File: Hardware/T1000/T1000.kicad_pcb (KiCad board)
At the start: 4 copper layers, 1 part, among them U4 MAX77857

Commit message: started layout
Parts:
- added AE1: Antenna, Terminator_Lib:ANT_1575AT_JOT-M, F.Cu at (83.6, 80.6)
- added B1: KMR2, Button_Switch_SMD:SW_Push_1P1T_NO_CK_KMR2, F.Cu at (54.8, 70.9)
- added B2: KMR2, Button_Switch_SMD:SW_Push_1P1T_NO_CK_KMR2, F.Cu at (54.8, 75.6)
- added BZ1: Buzzer, Terminator_Lib:PKMCS0909E4000-R1_MUR, F.Cu at (104.7, 102.7)
- added C1: 100nF, Capacitor_SMD:C_0402_1005Metric_Pad0.74x0.62mm_HandSolder, F.Cu at (98.4, 68.2)
- added C10: 100nF, Capacitor_SMD:C_0402_1005Metric_Pad0.74x0.62mm_HandSolder, F.Cu at (101.6, 70.1)
- added C11: 2.2uF, Capacitor_SMD:C_0603_1608Metric_Pad1.08x0.95mm_HandSolder, F.Cu at (80.2, 26.4)
- added C12: 100nF, Capacitor_SMD:C_0402_1005Metric_Pad0.74x0.62mm_HandSolder, F.Cu at (101.6, 72.1)
- added C13: 100nF, Capacitor_SMD:C_0402_1005Metric_Pad0.74x0.62mm_HandSolder, F.Cu at (101.6, 74.1)
- added C14: 100nF, Capacitor_SMD:C_0402_1005Metric_Pad0.74x0.62mm_HandSolder, F.Cu at (101.6, 76.0)
- added C15: 10uF, Capacitor_SMD:C_0603_1608Metric_Pad1.08x0.95mm_HandSolder, F.Cu at (80.2, 28.9)
- added C16: 100nF, Capacitor_SMD:C_0603_1608Metric_Pad1.08x0.95mm_HandSolder, F.Cu at (80.2, 31.4)
- added C17: 1uF, Capacitor_SMD:C_0603_1608Metric_Pad1.08x0.95mm_HandSolder, F.Cu at (80.2, 34.0)
- added C18: 10uF, Capacitor_SMD:C_0603_1608Metric_Pad1.08x0.95mm_HandSolder, F.Cu at (80.2, 36.5)
- added C19: 10uF, Capacitor_SMD:C_0603_1608Metric_Pad1.08x0.95mm_HandSolder, F.Cu at (80.2, 39.0)
- added C2: 22pF, Capacitor_SMD:C_0603_1608Metric_Pad1.08x0.95mm_HandSolder, F.Cu at (80.2, 21.4)
- added C20: 10uF, Capacitor_SMD:C_0603_1608Metric_Pad1.08x0.95mm_HandSolder, F.Cu at (80.2, 41.5)
- added C21: 100nF, Capacitor_SMD:C_0603_1608Metric_Pad1.08x0.95mm_HandSolder, F.Cu at (80.2, 44.0)
- added C22: 220nF, Capacitor_SMD:C_0603_1608Metric_Pad1.08x0.95mm_HandSolder, F.Cu at (80.2, 46.5)
- added C23: 220nF, Capacitor_SMD:C_0603_1608Metric_Pad1.08x0.95mm_HandSolder, F.Cu at (80.2, 49.0)
- added C24: 10pF, Capacitor_SMD:C_0603_1608Metric_Pad1.08x0.95mm_HandSolder, F.Cu at (84.5, 21.4)
- added C25: 2.2uF, Capacitor_SMD:C_0603_1608Metric_Pad1.08x0.95mm_HandSolder, F.Cu at (84.5, 23.9)
- added C26: 470nF, Capacitor_SMD:C_0603_1608Metric_Pad1.08x0.95mm_HandSolder, F.Cu at (84.5, 26.4)
- added C27: 10uF, Capacitor_SMD:C_0603_1608Metric_Pad1.08x0.95mm_HandSolder, F.Cu at (84.5, 28.9)
- added C28: 10uF, Capacitor_SMD:C_0603_1608Metric_Pad1.08x0.95mm_HandSolder, F.Cu at (84.5, 31.4)
- added C29: 15uF, Capacitor_SMD:C_0603_1608Metric_Pad1.08x0.95mm_HandSolder, F.Cu at (84.5, 34.0)
- added C3: 22pF, Capacitor_SMD:C_0603_1608Metric_Pad1.08x0.95mm_HandSolder, F.Cu at (80.2, 23.9)
- added C30: 10uF, Capacitor_SMD:C_0603_1608Metric_Pad1.08x0.95mm_HandSolder, F.Cu at (84.5, 36.5)
- added C31: 2.2uF, Capacitor_SMD:C_0603_1608Metric_Pad1.08x0.95mm_HandSolder, F.Cu at (84.5, 39.0)
- added C32: 220nF, Capacitor_SMD:C_0603_1608Metric_Pad1.08x0.95mm_HandSolder, F.Cu at (165.8, 82.9)
- added C33: 220nF, Capacitor_SMD:C_0603_1608Metric_Pad1.08x0.95mm_HandSolder, F.Cu at (156.1, 82.9)
- added C34: 4.7uF, Capacitor_SMD:C_0603_1608Metric_Pad1.08x0.95mm_HandSolder, F.Cu at (161.7, 94.1)
- added C35: 100nF, Capacitor_SMD:C_0603_1608Metric_Pad1.08x0.95mm_HandSolder, F.Cu at (84.5, 49.0)
- added C36: 47pF, Capacitor_SMD:C_0603_1608Metric_Pad1.08x0.95mm_HandSolder, F.Cu at (88.9, 21.4)
- added C37: 8.2pF, Capacitor_SMD:C_0603_1608Metric_Pad1.08x0.95mm_HandSolder, F.Cu at (88.9, 23.9)
- added C38: 22nF, Capacitor_SMD:C_0603_1608Metric_Pad1.08x0.95mm_HandSolder, F.Cu at (88.9, 26.4)
- added C39: 22uF, Capacitor_SMD:C_0603_1608Metric_Pad1.08x0.95mm_HandSolder, F.Cu at (155.2, 86.3)
- added C4: 100nF, Capacitor_SMD:C_0402_1005Metric_Pad0.74x0.62mm_HandSolder, F.Cu at (98.4, 70.1)
- added C40: 22uF, Capacitor_SMD:C_0603_1608Metric_Pad1.08x0.95mm_HandSolder, F.Cu at (155.2, 87.9)
- added C41: 680p, Capacitor_SMD:C_0603_1608Metric_Pad1.08x0.95mm_HandSolder, F.Cu at (160.1, 95.0)
- added C42: 10uF, Capacitor_SMD:C_0603_1608Metric_Pad1.08x0.95mm_HandSolder, F.Cu at (165.1, 86.8)
- added C5: 1uF, Capacitor_SMD:C_0402_1005Metric_Pad0.74x0.62mm_HandSolder, F.Cu at (98.4, 72.1)
- added C6: 1uF, Capacitor_SMD:C_0402_1005Metric_Pad0.74x0.62mm_HandSolder, F.Cu at (98.4, 74.1)
- added C7: 100nF, Capacitor_SMD:C_0402_1005Metric_Pad0.74x0.62mm_HandSolder, F.Cu at (98.4, 76.0)
- added C8: 100nF, Capacitor_SMD:C_0402_1005Metric_Pad0.74x0.62mm_HandSolder, F.Cu at (98.4, 78.0)
- added C9: 100nF, Capacitor_SMD:C_0402_1005Metric_Pad0.74x0.62mm_HandSolder, F.Cu at (101.6, 68.2)
- added D1: LED, Diode_SMD:D_0603_1608Metric_Pad1.05x0.95mm_HandSolder, F.Cu at (99.0, 80.3)
- added D2: USBLC6-2SC6, PCM_Package_TO_SOT_SMD_AKL:SOT-23-6, F.Cu at (106.9, 36.0)
- added J1: USB_C_Receptacle_USB2.0, Connector_USB:USB_C_Receptacle_GCT_USB4085, F.Cu at (67.1, 58.5)
- added J2: SOICbite, Terminator_Lib:SOIC_clipProgSmall, F.Cu at (62.4, 81.0)
- added J3: XT30, Connector_AMASS:AMASS_XT30PW-M_1x02_P2.50mm_Horizontal, F.Cu at (103.9, 64.4)
- added J4: Nichrome, Connector_PinHeader_2.54mm:PinHeader_1x02_P2.54mm_Vertical, F.Cu at (105.5, 69.5)
- added JP1: SolderJumper_2_Open, Jumper:SolderJumper-2_P1.3mm_Open_TrianglePad1.0x1.5mm, F.Cu at (163.6, 97.6)
- added JP2: SolderJumper_2_Open, Jumper:SolderJumper-2_P1.3mm_Open_TrianglePad1.0x1.5mm, F.Cu at (163.6, 100.5)
- added L1: 1.5uH, Inductor_SMD:L_Vishay_IHLP-2020, F.Cu at (103.9, 30.2)
- added L2: 3.3uH, Terminator_Lib:L_Bourns_SRP1265A, F.Cu at (160.9, 75.5)
- added L3: 3.3uH, Terminator_Lib:L_Bourns_SRP1265A, F.Cu at (85.9, 71.3)
- added Q1: IRLML0060TRPBF, Package_TO_SOT_SMD:SOT-23-3, F.Cu at (102.3, 47.9)
- added R1: DNP, Resistor_SMD:R_0603_1608Metric_Pad0.98x0.95mm_HandSolder, F.Cu at (88.9, 36.5)
- added R10: 154k, Resistor_SMD:R_0603_1608Metric_Pad0.98x0.95mm_HandSolder, F.Cu at (93.2, 28.9)
- added R11: 10k, Resistor_SMD:R_0603_1608Metric_Pad0.98x0.95mm_HandSolder, F.Cu at (93.2, 31.4)
- added R12: 10k, Resistor_SMD:R_0603_1608Metric_Pad0.98x0.95mm_HandSolder, F.Cu at (93.2, 34.0)
- added R13: 10k, Resistor_SMD:R_0603_1608Metric_Pad0.98x0.95mm_HandSolder, F.Cu at (93.2, 36.5)
- added R14: 5.1k, Resistor_SMD:R_0603_1608Metric_Pad0.98x0.95mm_HandSolder, F.Cu at (93.2, 39.0)
- added R15: 5.1k, Resistor_SMD:R_0603_1608Metric_Pad0.98x0.95mm_HandSolder, F.Cu at (93.2, 41.5)
- added R16: 510k, Resistor_SMD:R_0603_1608Metric_Pad0.98x0.95mm_HandSolder, F.Cu at (93.2, 44.0)
- added R17: 16.9k, Resistor_SMD:R_0603_1608Metric_Pad0.98x0.95mm_HandSolder, F.Cu at (93.2, 46.5)
- added R18: 178k, Resistor_SMD:R_0603_1608Metric_Pad0.98x0.95mm_HandSolder, F.Cu at (93.2, 49.0)
- added R19: 20k, Resistor_SMD:R_0603_1608Metric_Pad0.98x0.95mm_HandSolder, F.Cu at (97.6, 21.4)
- added R2: 10k, Resistor_SMD:R_0603_1608Metric_Pad0.98x0.95mm_HandSolder, F.Cu at (88.9, 39.0)
- added R20: 100m, Resistor_SMD:R_0603_1608Metric_Pad0.98x0.95mm_HandSolder, F.Cu at (97.6, 23.9)
- added R21: 33, Resistor_SMD:R_0603_1608Metric_Pad0.98x0.95mm_HandSolder, F.Cu at (97.6, 26.4)
- added R22: 33, Resistor_SMD:R_0603_1608Metric_Pad0.98x0.95mm_HandSolder, F.Cu at (97.6, 28.9)
- added R23: 81.1k, Resistor_SMD:R_0603_1608Metric_Pad0.98x0.95mm_HandSolder, F.Cu at (156.1, 92.0)
- added R24: 75k, Resistor_SMD:R_0603_1608Metric_Pad0.98x0.95mm_HandSolder, F.Cu at (163.3, 94.1)
- added R25: 5m, Resistor_SMD:R_0603_1608Metric_Pad0.98x0.95mm_HandSolder, F.Cu at (155.5, 90.4)
- added R26: 154k, Resistor_SMD:R_0603_1608Metric_Pad0.98x0.95mm_HandSolder, F.Cu at (155.9, 95.8)
- added R27: 154k, Resistor_SMD:R_0603_1608Metric_Pad0.98x0.95mm_HandSolder, F.Cu at (155.9, 94.2)
- added R28: 56.2k, Resistor_SMD:R_0603_1608Metric_Pad0.98x0.95mm_HandSolder, F.Cu at (158.5, 95.0)
- added R29: 100, Resistor_SMD:R_0603_1608Metric_Pad0.98x0.95mm_HandSolder, F.Cu at (101.3, 109.4)
- added R3: 1M, Resistor_SMD:R_0603_1608Metric_Pad0.98x0.95mm_HandSolder, F.Cu at (88.9, 41.5)
- added R4: 715k, Resistor_SMD:R_0603_1608Metric_Pad0.98x0.95mm_HandSolder, F.Cu at (88.9, 44.0)
- added R5: 27, Resistor_SMD:R_0603_1608Metric_Pad0.98x0.95mm_HandSolder, F.Cu at (88.9, 46.5)
- added R6: 27, Resistor_SMD:R_0603_1608Metric_Pad0.98x0.95mm_HandSolder, F.Cu at (88.9, 49.0)
- added R7: 590, Resistor_SMD:R_0603_1608Metric_Pad0.98x0.95mm_HandSolder, F.Cu at (93.2, 21.4)
- added R8: 1k, Resistor_SMD:R_0603_1608Metric_Pad0.98x0.95mm_HandSolder, F.Cu at (93.2, 23.9)
- added R9: 1.05M, Resistor_SMD:R_0603_1608Metric_Pad0.98x0.95mm_HandSolder, F.Cu at (93.2, 26.4)
- added TP1: TestPoint, TestPoint:TestPoint_Pad_D1.0mm, F.Cu at (95.3, 68.7)
- added TP2: TestPoint, TestPoint:TestPoint_Keystone_5000-5004_Miniature, F.Cu at (91.0, 80.5)
- added TP3: TestPoint, TestPoint:TestPoint_Pad_D1.0mm, F.Cu at (95.3, 71.8)
- added TP4: TestPoint, TestPoint:TestPoint_Pad_D1.0mm, F.Cu at (95.3, 74.8)
- added TP5: TestPoint, TestPoint:TestPoint_Pad_D1.0mm, F.Cu at (95.3, 77.8)
- added TP6: TestPoint, TestPoint:TestPoint_Pad_D1.0mm, F.Cu at (95.3, 80.9)
- added U1: LT3120JV-PBF, Terminator_Lib:LQFN28_Rev0_ADI-M, F.Cu at (160.9, 88.8)
- added U2: RP2040, Terminator_Lib:RP2040-QFN-56, F.Cu at (30.8, 93.0)
- added U3: W25Q128JVS, Package_SO:SOIC-8_5.23x5.23mm_P1.27mm, F.Cu at (104.9, 23.5)
- added U5: MAX-M10S, RF_GPS:ublox_MAX, F.Cu at (57.9, 62.8)
- added U6: MS5607-02BA, Package_LGA:LGA-8_3x5mm_P1.25mm, F.Cu at (102.1, 36.9)
- added U7: LT6703CDC-3, PCM_Package_DFN_QFN_AKL:DFN-3-1EP-2x2mm_P0.5mm_EP1x1.35mm, F.Cu at (53.7, 79.8)
- added U8: MAX77857, Terminator_Lib:MAX77857-35WLP, F.Cu at (133.5, 57.8)
- added U9: XBee_SMT, RF_Module:Digi_XBee_SMT, F.Cu at (38.4, 35.7)
- added Y1: 445I23D12M00000, Crystal:Crystal_SMD_5032-2Pin_5.0x3.2mm, F.Cu at (71.0, 79.0)
- U4: value MAX77857 -> LTC4419; footprint Package_BGA:MAX77857-35WLP -> Package_SO:MSOP-12-1EP_3x4mm_P0.65mm_EP1.65x2.85mm_ThermalVias
- moved U4 62.0 mm to (103.4, 42.9)
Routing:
- net Net-(U1-ISN): track 0.00 -> 12.3 mm, vias 0 -> 2
- net GND: track 0.00 -> 9.27 mm
- net Net-(J4-Pin_1): track 0.00 -> 9.15 mm
- net Net-(U1-BST1): track 0.00 -> 6.04 mm
- net Net-(U1-BST2): track 0.00 -> 6.03 mm
- net Net-(U1-FB): track 0.00 -> 5.89 mm
- net +BATT: track 0.00 -> 4.85 mm
- net Net-(U1-VC): track 0.00 -> 3.35 mm
- net Net-(U1-PROG): track 0.00 -> 2.47 mm
- net Net-(U1-MPCC): track 0.00 -> 2.34 mm
- net Net-(U1-RT): track 0.00 -> 2.24 mm
- net Net-(C41-Pad1): track 0.00 -> 1.62 mm
- net (no net): track 0.63 -> 0.00 mm
- added copper zone on F.Cu, net Net-(C32-Pad2)
- added copper zone on F.Cu, net Net-(C33-Pad2)
- added copper zone on F.Cu, net Net-(J4-Pin_1)

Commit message: more layout
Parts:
- C1, C10, C12, C13, C14, C4, C5, C6, C7, C8, C9: moved to B.Cu
- C29: footprint Capacitor_SMD:C_0603_1608Metric_Pad1.08x0.95mm_HandSolder -> Capacitor_SMD:C_0805_2012Metric_Pad1.18x1.45mm_HandSolder
- L3: footprint Terminator_Lib:L_Bourns_SRP1265A -> Inductor_SMD:L_1008_2520Metric_Pad1.43x2.20mm_HandSolder
- R20: footprint Resistor_SMD:R_0603_1608Metric_Pad0.98x0.95mm_HandSolder -> Resistor_SMD:R_0805_2012Metric_Pad1.20x1.40mm_HandSolder
- moved U3 118.9 mm to (46.7, 127.2), turned to 90 degrees
- moved C15 91.5 mm to (50.0, 115.3), turned to 90 degrees
- moved C9 73.3 mm to (55.1, 124.8), turned to 90 degrees
- moved C13 69.0 mm to (50.6, 120.6)
- moved C12 69.0 mm to (50.6, 118.6)
- moved C5 68.8 mm to (50.6, 121.6)
- moved C4 68.8 mm to (50.6, 119.6)
- moved L3 68.4 mm to (145.4, 37.7)
- moved C10 68.0 mm to (53.3, 118.0), turned to -90 degrees
- moved C8 66.2 mm to (51.5, 124.8), turned to 90 degrees
- moved C1 66.1 mm to (57.5, 120.1), turned to 180 degrees
- moved C6 63.7 mm to (52.3, 118.0), turned to -90 degrees
- moved C14 62.6 mm to (55.1, 118.0), turned to -90 degrees
- moved C23 61.7 mm to (141.3, 40.6), turned to 180 degrees
- moved C29 61.4 mm to (145.6, 40.2), turned to 180 degrees
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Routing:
- net /QSPI_SS: track 0.00 -> 16.5 mm
- net /QSPI_SD1: track 0.00 -> 14.0 mm
- net Net-(C23-Pad1): track 0.00 -> 13.8 mm, vias 0 -> 13
- net Net-(C22-Pad2): track 0.00 -> 13.8 mm, vias 0 -> 13
- net /QSPI_SD2: track 0.00 -> 9.34 mm
- net Net-(U8-FB): track 0.00 -> 6.11 mm
- net Net-(U8-SEL): track 0.00 -> 6.10 mm
- net +3V3: track 0.00 -> 5.75 mm, vias 0 -> 2
- net /QSPI_SD3: track 0.00 -> 5.45 mm
- net +1V1: track 0.00 -> 4.54 mm, vias 0 -> 2
- net /QSPI_SCLK: track 0.00 -> 3.94 mm
- net GND: track 9.27 -> 12.1 mm
- net /QSPI_SD0: track 0.00 -> 2.37 mm
- net Net-(C24-Pad1): track 0.00 -> 1.62 mm
- net /LVC: track 0.00 -> 0.40 mm, vias 0 -> 1
- added copper zone on F.Cu, net +3V3
- added copper zone on F.Cu, net +VDC
- added copper zone on F.Cu, net GND
- added copper zone on F.Cu, net Net-(C22-Pad2)
- added copper zone on In1.Cu, net Net-(C22-Pad2)
- added copper zone on F.Cu, net Net-(C23-Pad1)
- added copper zone on In1.Cu, net Net-(C23-Pad1)
- added copper zone on F.Cu, net Net-(C24-Pad1)
- added copper zone on F.Cu, net Net-(JP1-B)
- added copper zone on F.Cu, net Net-(U1-ISN)
- added copper zone on F.Cu, net Net-(U8-BST1)
- added copper zone on F.Cu, net Net-(U8-BST2)
- added copper zone on F.Cu, net Net-(U8-SCL)

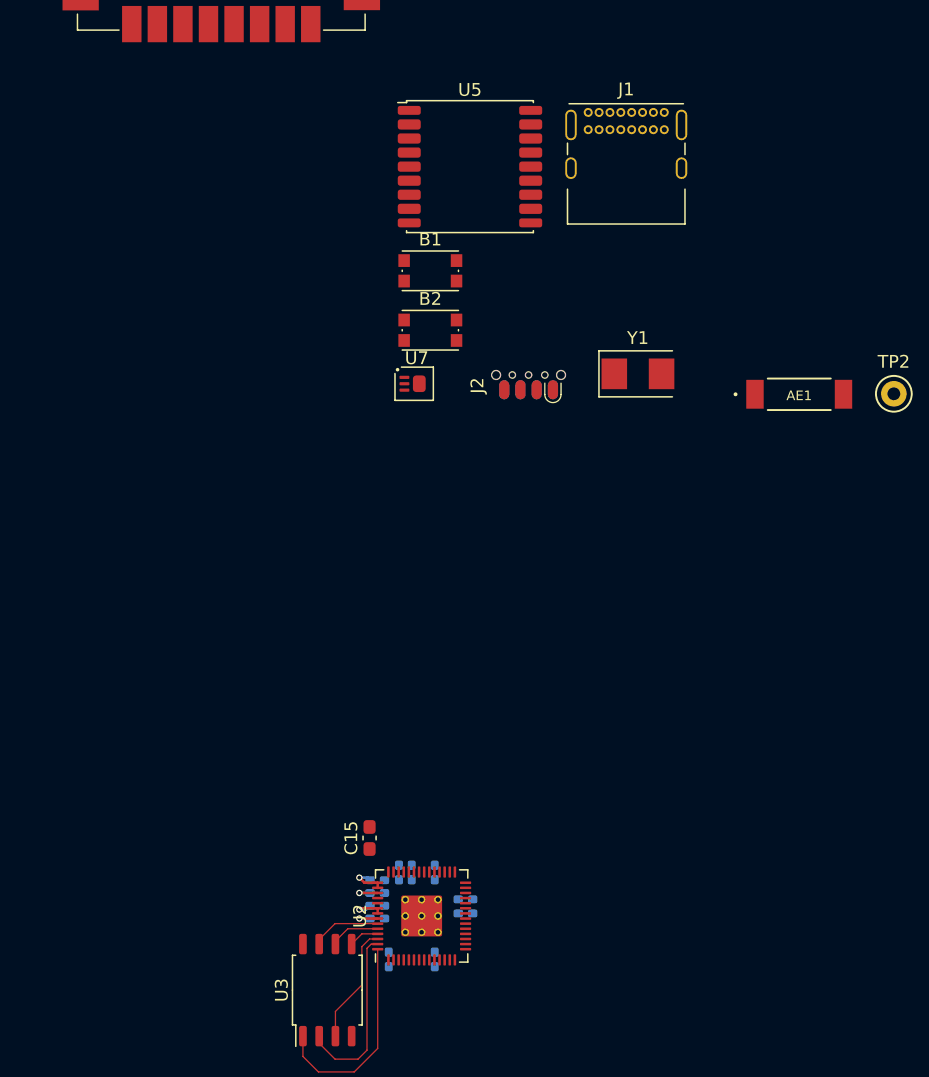
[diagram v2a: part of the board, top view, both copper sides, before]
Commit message: little bit of routing, changed to MIA-M10 GPS to make my life harder
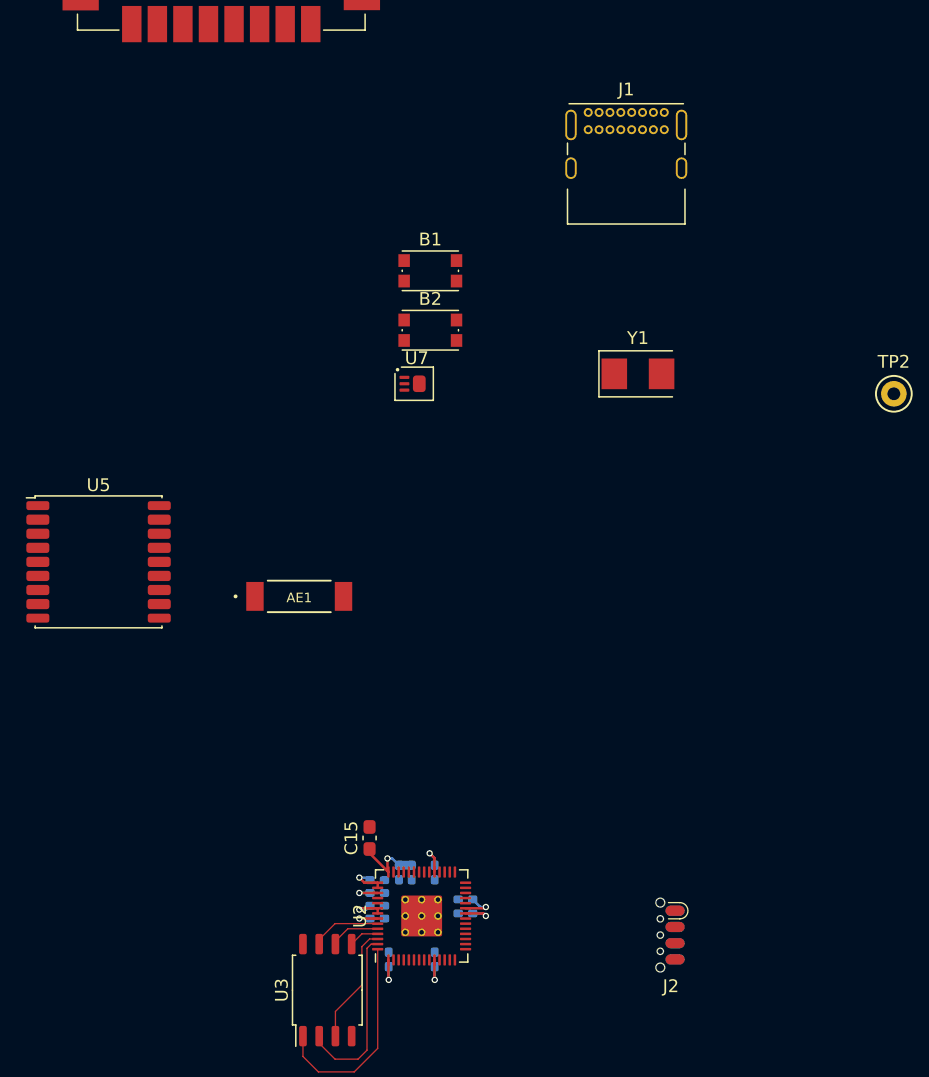
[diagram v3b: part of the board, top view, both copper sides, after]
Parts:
- moved J2 43.7 mm to (74.7, 122.9), turned to 90 degrees
- moved U5 42.4 mm to (28.8, 93.7)
- moved AE1 42.2 mm to (44.5, 96.4)
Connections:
- U2 pad 24: Net-(J2-Pin_2) -> Net-(J2-Pin_3)
- U2 pad 25: Net-(J2-Pin_3) -> Net-(J2-Pin_2)
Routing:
- net +3V3: track 5.75 -> 22.1 mm, vias 2 -> 7
- net +1V1: track 4.54 -> 7.45 mm, vias 2 -> 3
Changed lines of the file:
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@@
   )
   (footprint "Terminator_Lib:SOIC_clipProgSmall" (layer "F.Cu")
-    (at 62.44 80.985)
+    (at 74.65 122.895 90)
     (property "Sheetfile" "T1000.kicad_sch")
     (property "Sheetname" "")
@@
     (property "ki_keywords" "connector")
     (attr through_hole)
-    (fp_text reference "J2" (at -4 -1.0795 -90) (layer "F.SilkS")
+    (fp_text reference "J2" (at -4 -1.0795) (layer "F.SilkS")
         (effects (font (size 1 1) (thickness 0.25)))
     )
-    (fp_text value "SOICbite" (at 0.127 1.397 -180) (layer "F.Fab")
+    (fp_text value "SOICbite" (at 0.127 1.397 90) (layer "F.Fab")
         (effects (font (size 1 1) (thickness 0.15)))
     )
@@
     (fp_line (start 3.175 0.381) (end 3.175 -2.54)
       (stroke (width 0.1) (type solid)) (layer "F.Fab"))
-    (pad "" np_thru_hole circle (at -2.54 -1.905) (size 0.7 0.7) (drill 0.7) (layers "*.Cu" "*.Mask"))
-    (pad "" np_thru_hole circle (at -1.27 -1.905) (size 0.5 0.5) (drill 0.5) (layers "F&B.Cu" "*.Mask"))
-    (pad "" np_thru_hole circle (at 0 -1.905) (size 0.5 0.5) (drill 0.5) (layers "F&B.Cu" "*.Mask"))
-    (pad "" np_thru_hole circle (at 1.27 -1.905) (size 0.5 0.5) (drill 0.5) (layers "F&B.Cu" "*.Mask"))
-    (pad "" np_thru_hole circle (at 2.54 -1.905) (size 0.7 0.7) (drill 0.7) (layers "*.Cu" "*.Mask"))
-    (pad "1" smd oval (at 1.905 -0.75) (size 0.8 1.5) (layers "F.Cu" "F.Mask")
+    (pad "" np_thru_hole circle (at -2.54 -1.905 90) (size 0.7 0.7) (drill 0.7) (layers "*.Cu" "*.Mask"))
+    (pad "" np_thru_hole circle (at -1.27 -1.905 90) (size 0.5 0.5) (drill 0.5) (layers "F&B.Cu" "*.Mask"))
+    (pad "" np_thru_hole circle (at 0 -1.905 90) (size 0.5 0.5) (drill 0.5) (layers "F&B.Cu" "*.Mask"))
+    (pad "" np_thru_hole circle (at 1.27 -1.905 90) (size 0.5 0.5) (drill 0.5) (layers "F&B.Cu" "*.Mask"))
+    (pad "" np_thru_hole circle (at 2.54 -1.905 90) (size 0.7 0.7) (drill 0.7) (layers "*.Cu" "*.Mask"))
+    (pad "1" smd oval (at 1.905 -0.75 90) (size 0.8 1.5) (layers "F.Cu" "F.Mask")
       (net 8 "+3V3") (pinfunction "Pin_1") (pintype "passive"))
-    (pad "2" smd oval (at 0.635 -0.75) (size 0.8 1.5) (layers "F.Cu" "F.Mask")
+    (pad "2" smd oval (at 0.635 -0.75 90) (size 0.8 1.5) (layers "F.Cu" "F.Mask")
       (net 37 "Net-(J2-Pin_2)") (pinfunction "Pin_2") (pintype "passive"))
-    (pad "3" smd oval (at -0.635 -0.75) (size 0.8 1.5) (layers "F.Cu" "F.Mask")
+    (pad "3" smd oval (at -0.635 -0.75 90) (size 0.8 1.5) (layers "F.Cu" "F.Mask")
       (net 38 "Net-(J2-Pin_3)") (pinfunction "Pin_3") (pintype "passive"))
-    (pad "4" smd oval (at -1.905 -0.75) (size 0.8 1.5) (layers "F.Cu" "F.Mask")
+    (pad "4" smd oval (at -1.905 -0.75 90) (size 0.8 1.5) (layers "F.Cu" "F.Mask")
       (net 2 "GND") (pinfunction "Pin_4") (pintype "passive"))
-    (pad "5" smd oval (at -1.905 -0.75) (size 0.8 1.5) (layers "B.Cu" "B.Mask")
+    (pad "5" smd oval (at -1.905 -0.75 90) (size 0.8 1.5) (layers "B.Cu" "B.Mask")
       (net 39 "unconnected-(J2-Pin_5-Pad5)") (pinfunction "Pin_5") (pintype "passive+no_connect"))
-    (pad "6" smd oval (at -0.635 -0.75) (size 0.8 1.5) (layers "B.Cu" "B.Mask")
+    (pad "6" smd oval (at -0.635 -0.75 90) (size 0.8 1.5) (layers "B.Cu" "B.Mask")
       (net 40 "unconnected-(J2-Pin_6-Pad6)") (pinfunction "Pin_6") (pintype "passive+no_connect"))
-    (pad "7" smd oval (at 0.635 -0.75) (size 0.8 1.5) (layers "B.Cu" "B.Mask")
+    (pad "7" smd oval (at 0.635 -0.75 90) (size 0.8 1.5) (layers "B.Cu" "B.Mask")
       (net 41 "unconnected-(J2-Pin_7-Pad7)") (pinfunction "Pin_7") (pintype "passive+no_connect"))
-    (pad "8" smd oval (at 1.905 -0.75) (size 0.8 1.5) (layers "B.Cu" "B.Mask")
+    (pad "8" smd oval (at 1.905 -0.75 90) (size 0.8 1.5) (layers "B.Cu" "B.Mask")
       (net 42 "unconnected-(J2-Pin_8-Pad8)") (pinfunction "Pin_8") (pintype "passive+no_connect"))
   )
@@
       (net 5 "+1V1") (pinfunction "DVDD") (pintype "power_in"))
     (pad "24" smd roundrect (at 1 3.4375 90) (size 0.2 0.875) (layers "F.Cu" "F.Paste" "F.Mask") (roundrect_rratio 0.25)
-      (net 37 "Net-(J2-Pin_2)") (pinfunction "SWCLK") (pintype "output"))
+      (net 38 "Net-(J2-Pin_3)") (pinfunction "SWCLK") (pintype "output"))
     (pad "25" smd roundrect (at 1.4 3.4375 90) (size 0.2 0.875) (layers "F.Cu" "F.Paste" "F.Mask") (roundrect_rratio 0.25)
-      (net 38 "Net-(J2-Pin_3)") (pinfunction "SWD") (pintype "bidirectional"))
+      (net 37 "Net-(J2-Pin_2)") (pinfunction "SWD") (pintype "bidirectional"))
     (pad "26" smd roundrect (at 1.8 3.4375 90) (size 0.2 0.875) (layers "F.Cu" "F.Paste" "F.Mask") (roundrect_rratio 0.25)
       (net 3 "Net-(U2-RUN)") (pinfunction "RUN") (pintype "input"))
@@
   )
   (footprint "RF_GPS:ublox_MAX" (layer "F.Cu")
-    (at 57.855 62.78)
+    (at 28.8 93.7)
     (descr "ublox MAX 6/7/8, (https://www.u-blox.com/sites/default/files/MAX-8-M8-FW3_HardwareIntegrationManual_%28UBX-15030059%29.pdf)")
     (tags "GPS ublox MAX 6/7/8")
@@
   )
   (footprint "Terminator_Lib:ANT_1575AT_JOT-M" (layer "F.Cu")
-    (at 83.613499 80.5891)
+    (at 44.5 96.4)
     (tags "1575AT43A0040E ")
     (property "Sheetfile" "T1000.kicad_sch")
@@
       (polygon
         (pts
-          (xy 80.882999 79.535)
-          (xy 86.343999 79.535)
-          (xy 86.343999 81.6432)
-          (xy 80.882999 81.6432)
+          (xy 41.7695 95.3459)
+          (xy 47.2305 95.3459)
+          (xy 47.2305 97.4541)
+          (xy 41.7695 97.4541)
         )
       )
@@
   (segment (start 161.2 89.1) (end 160.95 88.85) (width 0.1) (layer "F.Cu") (net 2))
   (segment (start 50.6375 119.6) (end 49.2 119.6) (width 0.2) (layer "F.Cu") (net 5))
+  (segment (start 59 120.8) (end 59.1 120.7) (width 0.2) (layer "F.Cu") (net 5))
+  (segment (start 57.5125 120.8) (end 59 120.8) (width 0.2) (layer "F.Cu") (net 5))
   (segment (start 50.6375 121.6) (end 49.2 121.6) (width 0.2) (layer "F.Cu") (net 5))
   (via (at 49.2 121.6) (size 0.5) (drill 0.3) (layers "F.Cu" "B.Cu") (net 5))
+  (via (at 59.1 120.7) (size 0.5) (drill 0.3) (layers "F.Cu" "B.Cu") (net 5))
   (via (at 49.2 119.6) (size 0.5) (drill 0.3) (layers "F.Cu" "B.Cu") (net 5))
+  (segment (start 58.6675 120.7) (end 58.0675 120.1) (width 0.2) (layer "B.Cu") (net 5))
   (segment (start 49.2 119.6) (end 50.0325 119.6) (width 0.2) (layer "B.Cu") (net 5))
+  (segment (start 59.1 120.7) (end 58.6675 120.7) (width 0.2) (layer "B.Cu") (net 5))
   (segment (start 49.2 121.6) (end 50.0325 121.6) (width 0.2) (layer "B.Cu") (net 5))
+  (segment (start 51.4 117.8875) (end 51.4 116.9) (width 0.2) (layer "F.Cu") (net 8))
   (segment (start 50.6375 118.8) (end 49.6 118.8) (width 0.2) (layer "F.Cu") (net 8))
+  (segment (start 50 116.4875) (end 50 116.1625) (width 0.2) (layer "F.Cu") (net 8))
+  (segment (start 51.475 117.9625) (end 50 116.4875) (width 0.2) (layer "F.Cu") (net 8))
   (segment (start 49.6 118.8) (end 49.2 118.4) (width 0.2) (layer "F.Cu") (net 8))
   (segment (start 50.6375 121.2) (end 50.6375 120.8) (width 0.2) (layer "F.Cu") (net 8))
   (segment (start 50.6375 120.8) (end 49.3 120.8) (width 0.2) (layer "F.Cu") (net 8))
+  (segment (start 54.7 116.5) (end 55.075 116.875) (width 0.2) (layer "F.Cu") (net 8))
+  (segment (start 51.475 126.375) (end 51.5 126.4) (width 0.2) (layer "F.Cu") (net 8))
+  (segment (start 55.075 116.875) (end 55.075 117.9625) (width 0.2) (layer "F.Cu") (net 8))
+  (segment (start 59.1 121.4) (end 58.9 121.2) (width 0.2) (layer "F.Cu") (net 8))
+  (segment (start 51.475 117.9625) (end 51.4 117.8875) (width 0.2) (layer "F.Cu") (net 8))
   (segment (start 50.6375 119.2) (end 50.6375 118.8) (width 0.2) (layer "F.Cu") (net 8))
+  (segment (start 55.075 126.375) (end 55.1 126.4) (width 0.2) (layer "F.Cu") (net 8))
+  (segment (start 55.075 124.8375) (end 55.075 126.375) (width 0.2) (layer "F.Cu") (net 8))
+  (segment (start 51.475 124.8375) (end 51.475 126.375) (width 0.2) (layer "F.Cu") (net 8))
   (segment (start 49.3 120.8) (end 49.2 120.9) (width 0.2) (layer "F.Cu") (net 8))
+  (segment (start 58.9 121.2) (end 57.5125 121.2) (width 0.2) (layer "F.Cu") (net 8))
+  (via (at 55.1 126.4) (size 0.5) (drill 0.3) (layers "F.Cu" "B.Cu") (net 8))
+  (via (at 51.4 116.9) (size 0.5) (drill 0.3) (layers "F.Cu" "B.Cu") (net 8))
   (via (at 49.2 120.9) (size 0.5) (drill 0.3) (layers "F.Cu" "B.Cu") (net 8))
+  (via (at 54.7 116.5) (size 0.5) (drill 0.3) (layers "F.Cu" "B.Cu") (net 8))
+  (via (at 51.5 126.4) (size 0.5) (drill 0.3) (layers "F.Cu" "B.Cu") (net 8))
   (via (at 49.2 118.4) (size 0.5) (drill 0.3) (layers "F.Cu" "B.Cu") (net 8))
+  (via (at 59.1 121.4) (size 0.5) (drill 0.3) (layers "F.Cu" "B.Cu") (net 8))
+  (segment (start 59.1 121.4) (end 58.9 121.2) (width 0.2) (layer "B.Cu") (net 8))
+  (segment (start 55.1 126.4) (end 55.1 125.3675) (width 0.2) (layer "B.Cu") (net 8))
+  (segment (start 58.9 121.2) (end 58.0675 121.2) (width 0.2) (layer "B.Cu") (net 8))
+  (segment (start 51.4 116.9) (end 51.7675 116.9) (width 0.2) (layer "B.Cu") (net 8))
+  (segment (start 51.5 126.4) (end 51.5 125.3675) (width 0.2) (layer "B.Cu") (net 8))
+  (segment (start 54.7 116.5) (end 55.1 116.9) (width 0.2) (layer "B.Cu") (net 8))
+  (segment (start 53.3 117.4325) (end 52.3 117.4325) (width 0.7) (layer "B.Cu") (net 8))
   (segment (start 49.2 120.9) (end 49.7325 120.9) (width 0.2) (layer "B.Cu") (net 8))
+  (segment (start 51.7675 116.9) (end 52.3 117.4325) (width 0.2) (layer "B.Cu") (net 8))
   (segment (start 49.7325 120.9) (end 50.0325 120.6) (width 0.2) (layer "B.Cu") (net 8))
   (segment (start 49.2 118.4) (end 49.8325 118.4) (width 0.2) (layer "B.Cu") (net 8))
+  (segment (start 55.1 116.9) (end 55.1 117.4325) (width 0.2) (layer "B.Cu") (net 8))
   (segment (start 49.8325 118.4) (end 50.0325 118.6) (width 0.2) (layer "B.Cu") (net 8))
   (segment (start 158.900002 89.1) (end 155.8875 89.1) (width 0.1) (layer "F.Cu") (net 9))
